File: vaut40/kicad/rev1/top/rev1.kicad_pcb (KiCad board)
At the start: 2 copper layers, 228.3 x 128.1 mm, 40 parts, among them SW1 SW_PUSH, SW10 SW_PUSH, SW11 SW_PUSH, SW12 SW_PUSH, SW13 SW_PUSH, SW14 SW_PUSH, SW15 SW_PUSH, SW16 SW_PUSH, SW17 SW_PUSH, SW18 SW_PUSH, SW19 SW_PUSH, SW2 SW_PUSH, SW20 SW_PUSH, SW21 SW_PUSH, SW22 SW_PUSH, SW23 SW_PUSH, SW24 SW_PUSH, SW25 SW_PUSH, SW26 SW_PUSH, SW27 SW_PUSH, SW28 SW_PUSH, SW29 SW_PUSH, SW3 SW_PUSH, SW30 SW_PUSH, SW31 SW_PUSH, SW32 SW_PUSH, SW33 SW_PUSH, SW34 SW_PUSH, SW35 SW_PUSH, SW36 SW_PUSH, SW37 SW_PUSH, SW38 SW_PUSH, SW39 SW_PUSH, SW4 SW_PUSH, SW40 SW_PUSH, SW5 SW_PUSH, SW6 SW_PUSH, SW7 SW_PUSH, SW8 SW_PUSH, SW9 SW_PUSH

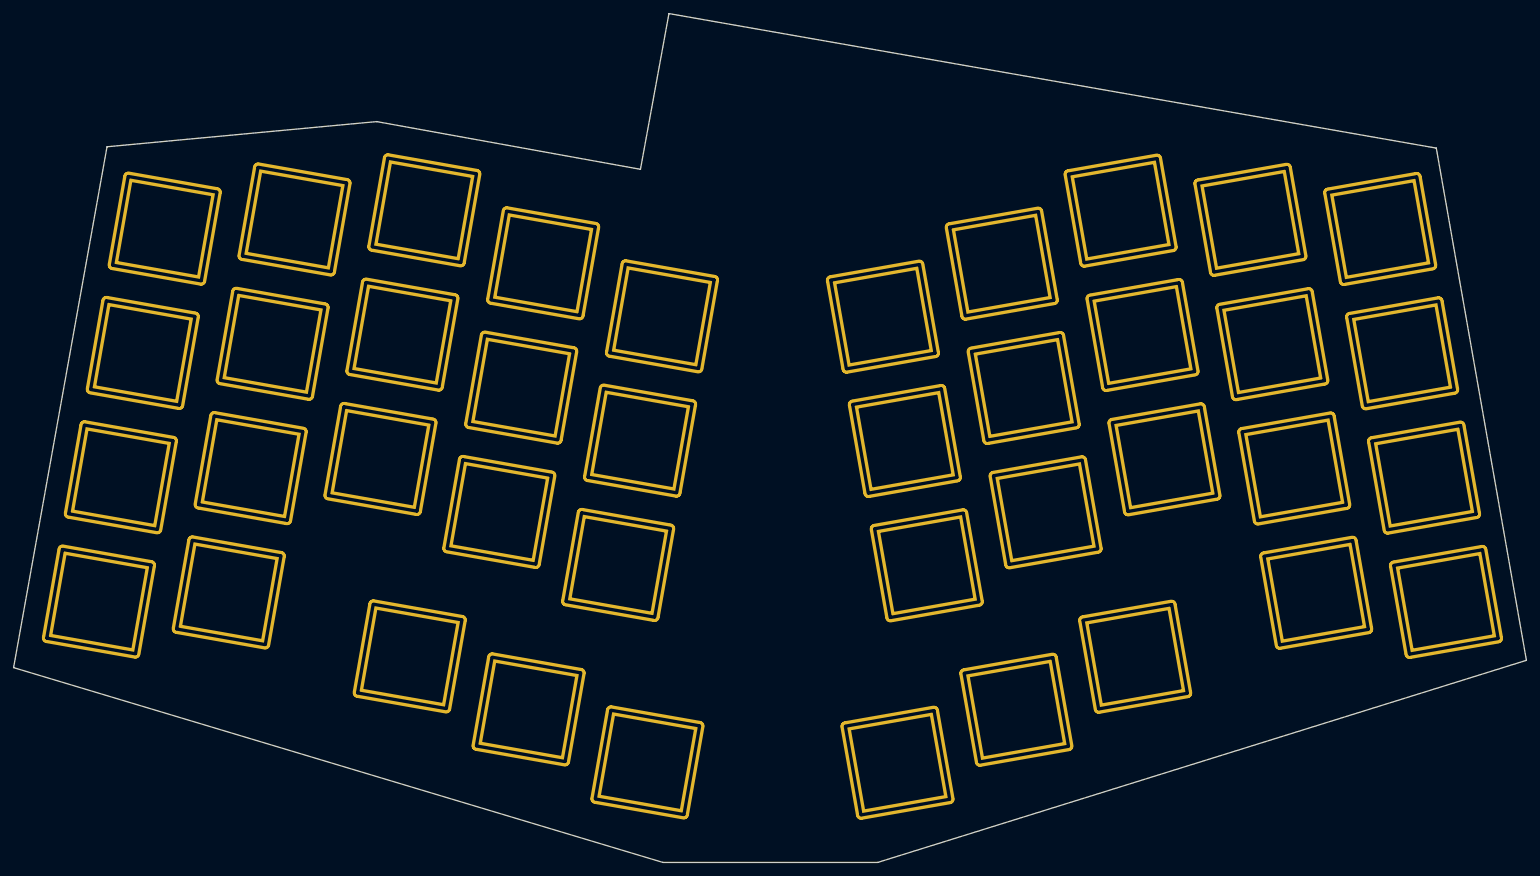
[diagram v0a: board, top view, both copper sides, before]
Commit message: add hole of top
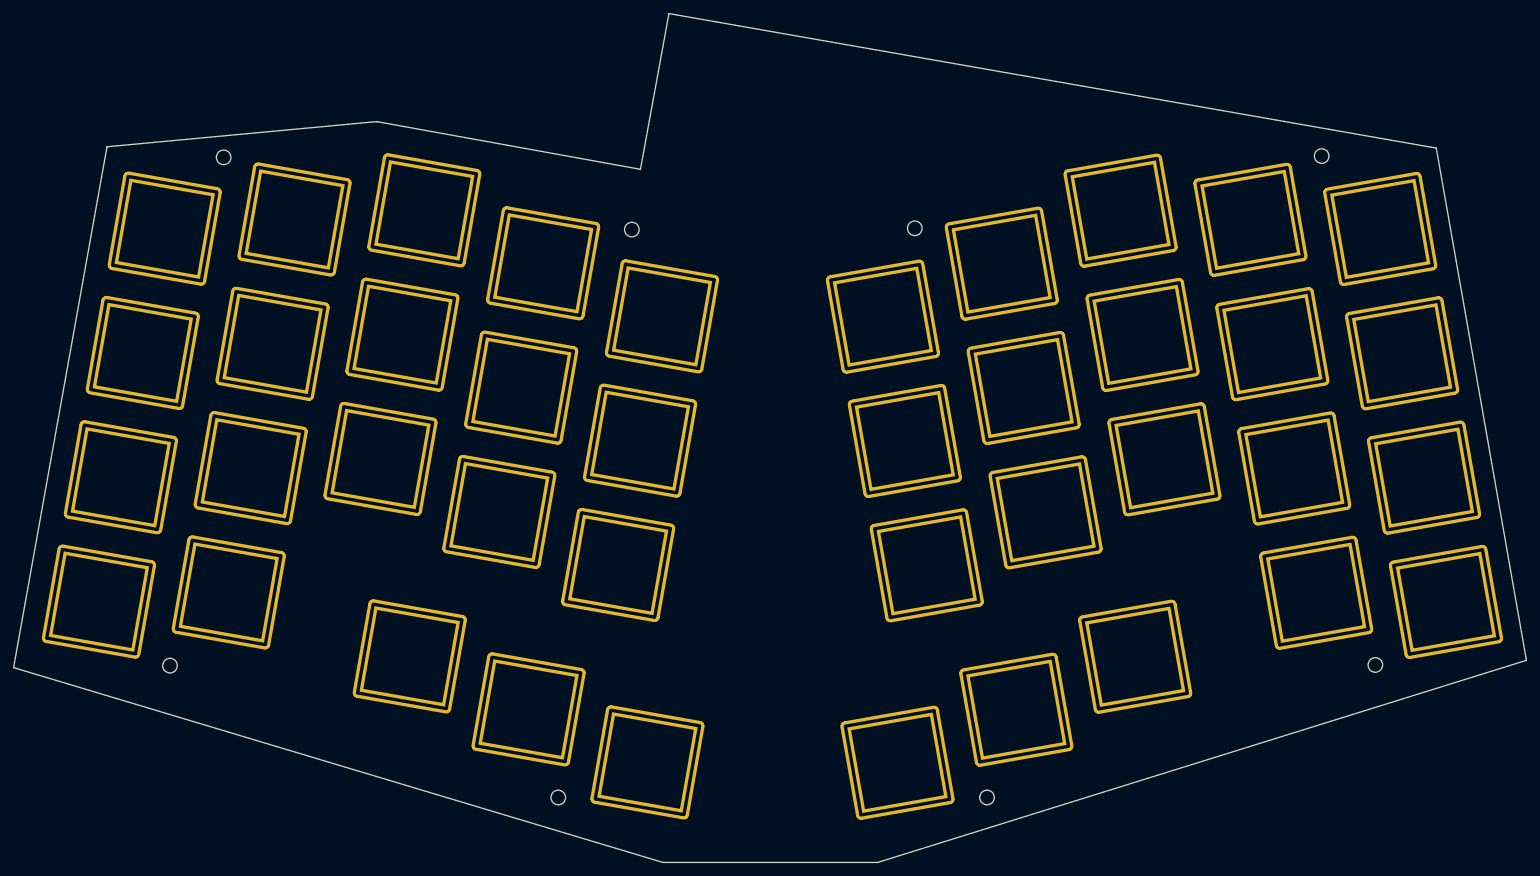
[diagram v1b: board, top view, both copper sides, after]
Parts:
- added Ref**: Val**, kbd_Hole:m2_Screw_Hole, F.Cu at (245.2, 123.8)
- added Ref**: Val**, kbd_Hole:m2_Screw_Hole, F.Cu at (63.3, 123.9)
- added Ref**: Val**, kbd_Hole:m2_Screw_Hole, F.Cu at (186.6, 143.8)
- added Ref**: Val**, kbd_Hole:m2_Screw_Hole, F.Cu at (237.1, 47.0)
- added Ref**: Val**, kbd_Hole:m2_Screw_Hole, F.Cu at (71.4, 47.2)
- added Ref**: Val**, kbd_Hole:m2_Screw_Hole, F.Cu at (133.0, 58.1)
- added Ref**: Val**, kbd_Hole:m2_Screw_Hole, F.Cu at (175.7, 57.9)
- added Ref**: Val**, kbd_Hole:m2_Screw_Hole, F.Cu at (121.9, 143.8)
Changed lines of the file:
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@@
       (net 5 "Column4") (pinfunction "1") (pintype "passive"))
+  )
+  (footprint "kbd_Hole:m2_Screw_Hole" (layer "F.Cu")
+    (at 245.2 123.8)
+    (descr "Mounting Hole 2.2mm, no annular, M2")
+    (tags "mounting hole 2.2mm no annular m2")
+    (attr exclude_from_pos_files exclude_from_bom)
+    (fp_text reference "Ref**" (at 0 -3.2) (layer "F.Fab")
+        (effects (font (size 1 1) (thickness 0.15)))
+    )
+    (fp_text value "Val**" (at 0 3.2) (layer "F.Fab")
+        (effects (font (size 1 1) (thickness 0.15)))
+    )
+    (fp_text user "${REFERENCE}" (at 0.3 0) (layer "F.Fab")
+        (effects (font (size 1 1) (thickness 0.15)))
+    )
+    (fp_circle (center 0 0) (end 2.2 0)
+      (stroke (width 0.15) (type solid)) (fill none) (layer "Cmts.User"))
+    (fp_circle (center 0 0) (end 2.45 0)
+      (stroke (width 0.05) (type solid)) (fill none) (layer "F.CrtYd"))
+    (pad "" np_thru_hole circle (at 0 0) (size 2.2 2.2) (drill 2.2) (layers "F&B.Cu" "*.Mask"))
   )
   (footprint "kbd:SW_Hole_TH" (layer "F.Cu")
@@
       (net 4 "Column3") (pinfunction "1") (pintype "passive"))
   )
+  (footprint "kbd_Hole:m2_Screw_Hole" (layer "F.Cu")
+    (at 63.3 123.9)
+    (descr "Mounting Hole 2.2mm, no annular, M2")
+    (tags "mounting hole 2.2mm no annular m2")
+    (attr exclude_from_pos_files exclude_from_bom)
+    (fp_text reference "Ref**" (at 0 -3.2) (layer "F.Fab")
+        (effects (font (size 1 1) (thickness 0.15)))
+    )
+    (fp_text value "Val**" (at 0 3.2) (layer "F.Fab")
+        (effects (font (size 1 1) (thickness 0.15)))
+    )
+    (fp_text user "${REFERENCE}" (at 0.3 0) (layer "F.Fab")
+        (effects (font (size 1 1) (thickness 0.15)))
+    )
+    (fp_circle (center 0 0) (end 2.2 0)
+      (stroke (width 0.15) (type solid)) (fill none) (layer "Cmts.User"))
+    (fp_circle (center 0 0) (end 2.45 0)
+      (stroke (width 0.05) (type solid)) (fill none) (layer "F.CrtYd"))
+    (pad "" np_thru_hole circle (at 0 0) (size 2.2 2.2) (drill 2.2) (layers "F&B.Cu" "*.Mask"))
+  )
+  (footprint "kbd_Hole:m2_Screw_Hole" (layer "F.Cu")
+    (at 186.6 143.8)
+    (descr "Mounting Hole 2.2mm, no annular, M2")
+    (tags "mounting hole 2.2mm no annular m2")
+    (attr exclude_from_pos_files exclude_from_bom)
+    (fp_text reference "Ref**" (at 0 -3.2) (layer "F.Fab")
+        (effects (font (size 1 1) (thickness 0.15)))
+    )
+    (fp_text value "Val**" (at 0 3.2) (layer "F.Fab")
+        (effects (font (size 1 1) (thickness 0.15)))
+    )
+    (fp_text user "${REFERENCE}" (at 0.3 0) (layer "F.Fab")
+        (effects (font (size 1 1) (thickness 0.15)))
+    )
+    (fp_circle (center 0 0) (end 2.2 0)
+      (stroke (width 0.15) (type solid)) (fill none) (layer "Cmts.User"))
+    (fp_circle (center 0 0) (end 2.45 0)
+      (stroke (width 0.05) (type solid)) (fill none) (layer "F.CrtYd"))
+    (pad "" np_thru_hole circle (at 0 0) (size 2.2 2.2) (drill 2.2) (layers "F&B.Cu" "*.Mask"))
+  )
   (footprint "kbd:SW_Hole_TH" (layer "F.Cu")
     (at 101.6838 55.1895 -10)
@@
       (net 10 "Column9") (pinfunction "1") (pintype "passive"))
   )
+  (footprint "kbd_Hole:m2_Screw_Hole" (layer "F.Cu")
+    (at 237.1 47)
+    (descr "Mounting Hole 2.2mm, no annular, M2")
+    (tags "mounting hole 2.2mm no annular m2")
+    (attr exclude_from_pos_files exclude_from_bom)
+    (fp_text reference "Ref**" (at 0 -3.2) (layer "F.Fab")
+        (effects (font (size 1 1) (thickness 0.15)))
+    )
+    (fp_text value "Val**" (at 0 3.2) (layer "F.Fab")
+        (effects (font (size 1 1) (thickness 0.15)))
+    )
+    (fp_text user "${REFERENCE}" (at 0.3 0) (layer "F.Fab")
+        (effects (font (size 1 1) (thickness 0.15)))
+    )
+    (fp_circle (center 0 0) (end 2.2 0)
+      (stroke (width 0.15) (type solid)) (fill none) (layer "Cmts.User"))
+    (fp_circle (center 0 0) (end 2.45 0)
+      (stroke (width 0.05) (type solid)) (fill none) (layer "F.CrtYd"))
+    (pad "" np_thru_hole circle (at 0 0) (size 2.2 2.2) (drill 2.2) (layers "F&B.Cu" "*.Mask"))
+  )
   (footprint "kbd:SW_Hole_TH" (layer "F.Cu")
     (at 130.935 108.707 -10)
@@
       (net 1 "Column0") (pinfunction "1") (pintype "passive"))
   )
+  (footprint "kbd_Hole:m2_Screw_Hole" (layer "F.Cu")
+    (at 71.4 47.2)
+    (descr "Mounting Hole 2.2mm, no annular, M2")
+    (tags "mounting hole 2.2mm no annular m2")
+    (attr exclude_from_pos_files exclude_from_bom)
+    (fp_text reference "Ref**" (at 0 -3.2) (layer "F.Fab")
+        (effects (font (size 1 1) (thickness 0.15)))
+    )
+    (fp_text value "Val**" (at 0 3.2) (layer "F.Fab")
+        (effects (font (size 1 1) (thickness 0.15)))
+    )
+    (fp_text user "${REFERENCE}" (at 0.3 0) (layer "F.Fab")
+        (effects (font (size 1 1) (thickness 0.15)))
+    )
+    (fp_circle (center 0 0) (end 2.2 0)
+      (stroke (width 0.15) (type solid)) (fill none) (layer "Cmts.User"))
+    (fp_circle (center 0 0) (end 2.45 0)
+      (stroke (width 0.05) (type solid)) (fill none) (layer "F.CrtYd"))
+    (pad "" np_thru_hole circle (at 0 0) (size 2.2 2.2) (drill 2.2) (layers "F&B.Cu" "*.Mask"))
+  )
   (footprint "kbd:SW_Hole_TH" (layer "F.Cu")
     (at 82.0962 56.5717 -10)
@@
       (net 4 "Column3") (pinfunction "1") (pintype "passive"))
   )
+  (footprint "kbd_Hole:m2_Screw_Hole" (layer "F.Cu")
+    (at 133 58.1)
+    (descr "Mounting Hole 2.2mm, no annular, M2")
+    (tags "mounting hole 2.2mm no annular m2")
+    (attr exclude_from_pos_files exclude_from_bom)
+    (fp_text reference "Ref**" (at 0 -3.2) (layer "F.Fab")
+        (effects (font (size 1 1) (thickness 0.15)))
+    )
+    (fp_text value "Val**" (at 0 3.2) (layer "F.Fab")
+        (effects (font (size 1 1) (thickness 0.15)))
+    )
+    (fp_text user "${REFERENCE}" (at 0.3 0) (layer "F.Fab")
+        (effects (font (size 1 1) (thickness 0.15)))
+    )
+    (fp_circle (center 0 0) (end 2.2 0)
+      (stroke (width 0.15) (type solid)) (fill none) (layer "Cmts.User"))
+    (fp_circle (center 0 0) (end 2.45 0)
+      (stroke (width 0.05) (type solid)) (fill none) (layer "F.CrtYd"))
+    (pad "" np_thru_hole circle (at 0 0) (size 2.2 2.2) (drill 2.2) (layers "F&B.Cu" "*.Mask"))
+  )
   (footprint "kbd:SW_Hole_TH" (layer "F.Cu")
     (at 95.0678 92.7107 -10)
@@
       (net 1 "Column0") (pinfunction "1") (pintype "passive"))
   )
-  (footprint "kbd:SW_Hole_TH" (layer "F.Cu")
+  (footprint "kbd_Hole:m2_Screw_Hole" (layer "F.Cu")
+    (at 175.7 57.9)
+    (descr "Mounting Hole 2.2mm, no annular, M2")
+    (tags "mounting hole 2.2mm no annular m2")
+    (attr exclude_from_pos_files exclude_from_bom)
+    (fp_text reference "Ref**" (at 0 -3.2) (layer "F.Fab")
+        (effects (font (size 1 1) (thickness 0.15)))
+    )
+    (fp_text value "Val**" (at 0 3.2) (layer "F.Fab")
+        (effects (font (size 1 1) (thickness 0.15)))
+    )
+    (fp_text user "${REFERENCE}" (at 0.3 0) (layer "F.Fab")
+        (effects (font (size 1 1) (thickness 0.15)))
+    )
+    (fp_circle (center 0 0) (end 2.2 0)
+      (stroke (width 0.15) (type solid)) (fill none) (layer "Cmts.User"))
+    (fp_circle (center 0 0) (end 2.45 0)
+      (stroke (width 0.05) (type solid)) (fill none) (layer "F.CrtYd"))
+    (pad "" np_thru_hole circle (at 0 0) (size 2.2 2.2) (drill 2.2) (layers "*.Cu" "*.Mask"))
+  )
+  (footprint "kbd_Hole:m2_Screw_Hole" (layer "F.Cu")
+    (at 121.9 143.8)
+    (descr "Mounting Hole 2.2mm, no annular, M2")
+    (tags "mounting hole 2.2mm no annular m2")
+    (attr exclude_from_pos_files exclude_from_bom)
+    (fp_text reference "Ref**" (at 0 -3.2) (layer "F.Fab")
+        (effects (font (size 1 1) (thickness 0.15)))
+    )
+    (fp_text value "Val**" (at 0 3.2) (layer "F.Fab")
+        (effects (font (size 1 1) (thickness 0.15)))
+    )
+    (fp_text user "${REFERENCE}" (at 0.3 0) (layer "F.Fab")
+        (effects (font (size 1 1) (thickness 0.15)))
+    )
+    (fp_circle (center 0 0) (end 2.2 0)
+      (stroke (width 0.15) (type solid)) (fill none) (layer "Cmts.User"))
+    (fp_circle (center 0 0) (end 2.45 0)
+      (stroke (width 0.05) (type solid)) (fill none) (layer "F.CrtYd"))
+    (pad "" np_thru_hole circle (at 0 0) (size 2.2 2.2) (drill 2.2) (layers "F&B.Cu" "*.Mask"))
+  )
+  (footprint "kbd:SW_Hole_TH" (layer "F.Cu")

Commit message: fix top plate
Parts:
- SW1, SW10, SW11, SW12, SW13, SW14, SW15, SW16, SW17, SW18, SW19, SW2, SW20, SW21, SW22, SW23, SW24, SW25, SW26, SW27, SW28, SW29, SW3, SW30, SW31, SW32, SW33, SW34, SW35, SW36, SW37, SW38, SW39, SW4, SW40, SW5, SW6, SW7, SW8, SW9: footprint kbd:SW_Hole_TH -> kbd:SW_Hole
